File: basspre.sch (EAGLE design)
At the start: 6 parts, among them IC1 LF351D

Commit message: initial layout
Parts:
- removed R1: 1M5, resistor:R-US_R0603
- removed U$1: LM4250, russell_random:LM4250
- added C102, C104, C107: 1uF, resistor:C-USC0603
- added C103: 1800 pF, resistor:C-USC0603
- added C105, C108: 120pf, resistor:C-USC0603
- added C106: 500pF, resistor:C-USC0603
- added C201, C202, C203, C204: .1uF, resistor:C-USC0603
- added R102: 220K, resistor:R-US_R0603
- added R103: 100K, resistor:R-US_R0603
- added R104: 1.5M, resistor:R-US_R0603
- added SV1: (no value), con-lstb:MA09-1
- added TP1, TP2, TP3: TPPAD1-13, testpad:TPPAD1-13
- added U103: LM4250, russell_random:LM4250
- R101: value 1M5 -> 1.5 M
- renumbered C1 to C101, IC1 to U102, R2 to R101, U$2 to U101
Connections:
- new net BASS1: C108.2, R103.2, SV1.5
- new net BASS2: C105.1, C106.2, C107.2, C108.1, SV1.4, TP3.TP, U103.OUT
- new net N$1: C102.1, C103.2, R102.2
- new net OUTPUT: C107.1, SV1.6
- new net TREBLE1: C106.1, SV1.3
- new net TREBLE2: C104.1, C105.2, R102.1, R103.1, SV1.2, U103.-IN
- new net TREBLE3: C103.1, SV1.1
- net GND: now also C104.2, C201.2, C202.2, C203.2, C204.2, R104.2, SV1.8, U103.V-; no longer R1.2, U$1.V-
- net INPUT: now also SV1.7
- net N$2: now also R104.1, U103.CURRENT; no longer R1.1, U$1.CURRENT
- net N$3: now also C102.2, TP2.TP
- net V+: now also C202.1, C203.1, C204.1, SV1.9, U103.V+; no longer U$1.V+
- net VGND: now also C201.1, TP1.TP, U103.+IN; no longer U$1.+IN
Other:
- note added: "Bypass"
- note added: "Connections"
- note added: "EQ"

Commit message: fix up values
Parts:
- C108: value 120pf -> 47nF
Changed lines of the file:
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@@
 <part name="C105" library="resistor" deviceset="C-US" device="C0603" value="120pf"/>
 <part name="R103" library="resistor" deviceset="R-US_" device="R0603" value="100K"/>
-<part name="C108" library="resistor" deviceset="C-US" device="C0603" value="120pf"/>
+<part name="C108" library="resistor" deviceset="C-US" device="C0603" value="47nF"/>
 <part name="C102" library="resistor" deviceset="C-US" device="C0603" value="1uF"/>
 <part name="R102" library="resistor" deviceset="R-US_" device="R0603" value="220K"/>

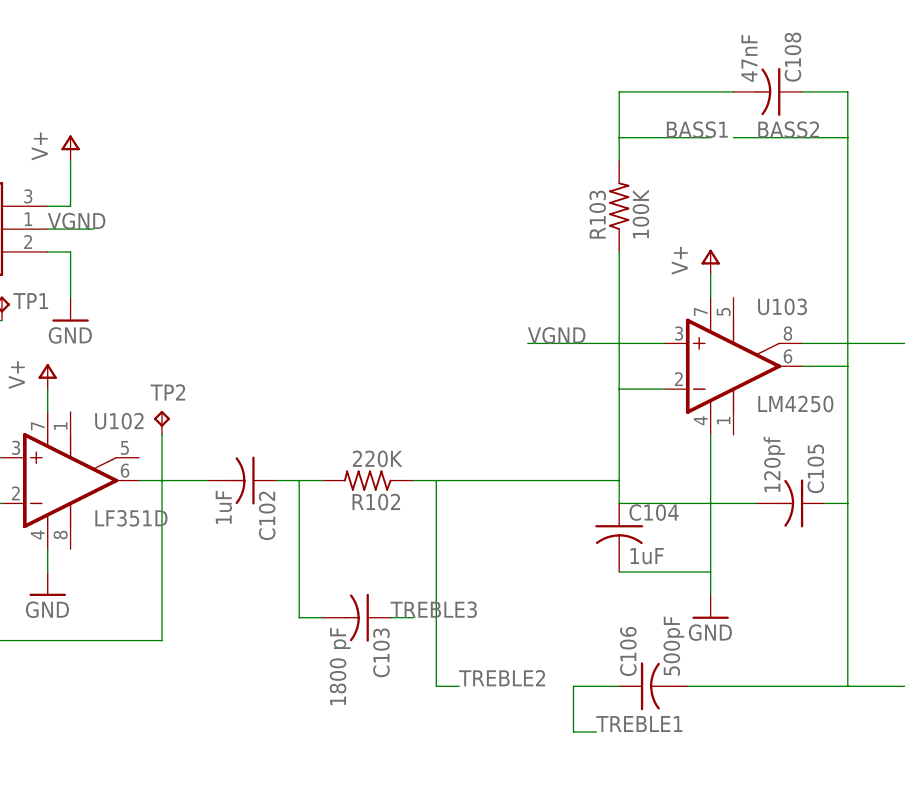
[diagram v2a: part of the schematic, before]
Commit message: added simulations, changed some values around
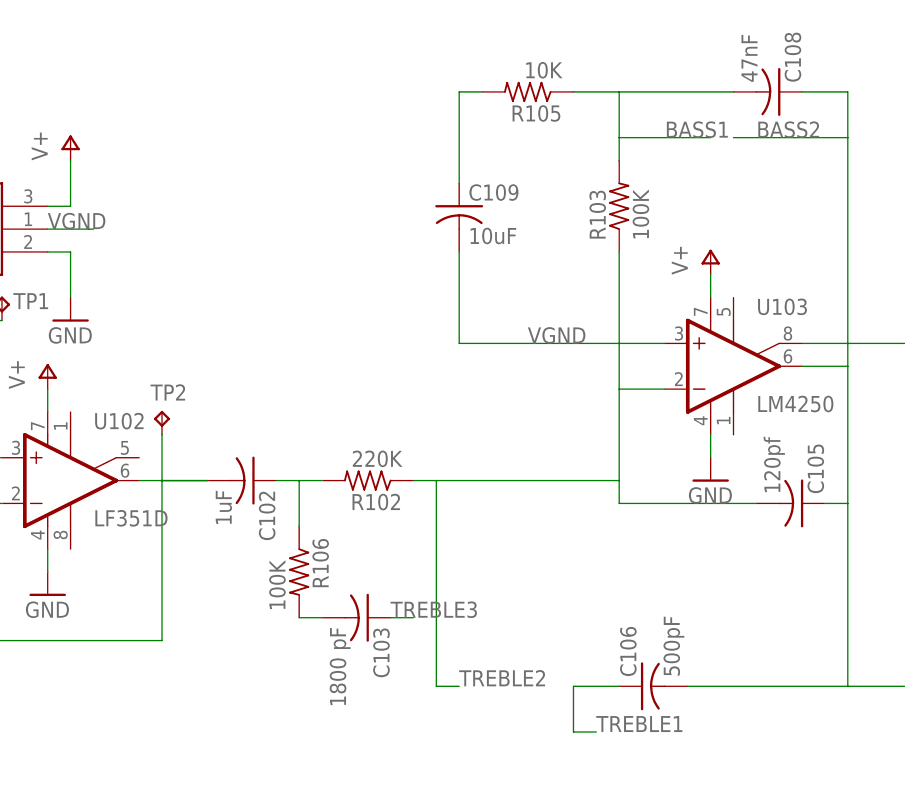
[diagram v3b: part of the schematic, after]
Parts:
- removed C104: 1uF, resistor:C-USC0603
- added C109: 10uF, resistor:C-USC0603
- added R105: 10K, resistor:R-US_R0603
- added R106: 100K, resistor:R-US_R0603
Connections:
- new net N$4: C109.1, R105.2
- new net N$5: C103.2, R106.2
- net BASS1: now also R105.1
- net GND: no longer C104.2
- net N$1: now also R106.1; no longer C103.2
- net TREBLE2: no longer C104.1
- net VGND: now also C109.2
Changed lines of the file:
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@@
 <part name="C101" library="resistor" deviceset="C-US" device="C0603" value="1uF"/>
 <part name="R101" library="resistor" deviceset="R-US_" device="R0603" value="1.5 M"/>
-<part name="C104" library="resistor" deviceset="C-US" device="C0603" value="1uF"/>
 <part name="C105" library="resistor" deviceset="C-US" device="C0603" value="120pf"/>
 <part name="R103" library="resistor" deviceset="R-US_" device="R0603" value="100K"/>
@@
 <part name="P+4" library="supply1" deviceset="V+" device=""/>
 <part name="GND6" library="supply1" deviceset="GND" device=""/>
+<part name="R105" library="resistor" deviceset="R-US_" device="R0603" value="10K"/>
+<part name="C109" library="resistor" deviceset="C-US" device="C0603" value="10uF"/>
+<part name="R106" library="resistor" deviceset="R-US_" device="R0603" value="100K"/>
 </parts>
 <sheets>
@@
 <instance part="U103" gate="G$1" x="114.3" y="149.86"/>
 <instance part="U101" gate="G$1" x="25.4" y="162.56"/>
-<instance part="GND2" gate="1" x="109.22" y="119.38"/>
+<instance part="GND2" gate="1" x="109.22" y="134.62"/>
 <instance part="P+2" gate="1" x="38.1" y="172.72"/>
 <instance part="P+1" gate="1" x="109.22" y="160.02"/>
@@
 <instance part="C101" gate="G$1" x="17.78" y="137.16" rot="R270"/>
 <instance part="R101" gate="G$1" x="25.4" y="144.78" rot="R90"/>
-<instance part="C104" gate="G$1" x="99.06" y="129.54"/>
 <instance part="C105" gate="G$1" x="119.38" y="132.08" rot="MR90"/>
 <instance part="R103" gate="G$1" x="99.06" y="165.1" rot="R90"/>
@@
 <instance part="P+4" gate="1" x="195.58" y="182.88"/>
 <instance part="GND6" gate="1" x="195.58" y="165.1"/>
+<instance part="R105" gate="G$1" x="88.9" y="177.8" rot="R180"/>
+<instance part="C109" gate="G$1" x="81.28" y="165.1"/>
+<instance part="R106" gate="G$1" x="63.5" y="124.46" smashed="yes" rot="R270">
+<attribute name="NAME" x="64.9986" y="128.27" size="1.778" layer="95" rot="R270"/>
+<attribute name="VALUE" x="60.198" y="125.73" size="1.778" layer="96" rot="R270"/>
+</instance>
 </instances>
 <busses>
@@
 <pinref part="GND2" gate="1" pin="GND"/>
 <pinref part="U103" gate="G$1" pin="V-"/>
-<wire x1="109.22" y1="121.92" x2="109.22" y2="124.46" width="0.1524" layer="91"/>
-<pinref part="C104" gate="G$1" pin="2"/>
-<wire x1="109.22" y1="124.46" x2="109.22" y2="139.7" width="0.1524" layer="91"/>
-<wire x1="99.06" y1="124.46" x2="109.22" y2="124.46" width="0.1524" layer="91"/>
+<wire x1="109.22" y1="137.16" x2="109.22" y2="139.7" width="0.1524" layer="91"/>
 </segment>
 <segment>
@@
 <segment>
 <pinref part="U103" gate="G$1" pin="+IN"/>
-<wire x1="104.14" y1="149.86" x2="88.9" y2="149.86" width="0.1524" layer="91"/>
+<wire x1="104.14" y1="149.86" x2="81.28" y2="149.86" width="0.1524" layer="91"/>
 <label x="88.9" y="149.86" size="1.778" layer="95"/>
+<pinref part="C109" gate="G$1" pin="2"/>
+<wire x1="81.28" y1="160.02" x2="81.28" y2="149.86" width="0.1524" layer="91"/>
 </segment>
 <segment>
@@
 <pinref part="TP2" gate="G$1" pin="TP"/>
 <wire x1="48.26" y1="134.62" x2="48.26" y2="139.7" width="0.1524" layer="91"/>
+<wire x1="48.26" y1="134.62" x2="53.34" y2="134.62" width="0.1524" layer="91"/>
 </segment>
 </net>
@@
 <pinref part="U103" gate="G$1" pin="-IN"/>
 <wire x1="104.14" y1="144.78" x2="99.06" y2="144.78" width="0.1524" layer="91"/>
-<pinref part="C104" gate="G$1" pin="1"/>
 <wire x1="99.06" y1="144.78" x2="99.06" y2="134.62" width="0.1524" layer="91"/>
 <pinref part="C105" gate="G$1" pin="2"/>
@@
 <wire x1="99.06" y1="172.72" x2="109.22" y2="172.72" width="0.1524" layer="91"/>
 <label x="104.14" y="172.72" size="1.778" layer="95"/>
+<pinref part="R105" gate="G$1" pin="1"/>
+<wire x1="99.06" y1="177.8" x2="93.98" y2="177.8" width="0.1524" layer="91"/>
 </segment>
 <segment>
@@
 <pinref part="R102" gate="G$1" pin="2"/>
 <wire x1="60.96" y1="134.62" x2="63.5" y2="134.62" width="0.1524" layer="91"/>
+<pinref part="R106" gate="G$1" pin="1"/>
 <wire x1="63.5" y1="134.62" x2="66.04" y2="134.62" width="0.1524" layer="91"/>
-<wire x1="63.5" y1="134.62" x2="63.5" y2="119.38" width="0.1524" layer="91"/>
-<pinref part="C103" gate="G$1" pin="2"/>
-<wire x1="63.5" y1="119.38" x2="66.04" y2="119.38" width="0.1524" layer="91"/>
+<wire x1="63.5" y1="129.54" x2="63.5" y2="134.62" width="0.1524" layer="91"/>
 </segment>
 </net>
@@
 </segment>
 </net>
+<net name="N$4" class="0">
+<segment>
+<pinref part="C109" gate="G$1" pin="1"/>
+<wire x1="81.28" y1="167.64" x2="81.28" y2="177.8" width="0.1524" layer="91"/>
+<pinref part="R105" gate="G$1" pin="2"/>
+<wire x1="81.28" y1="177.8" x2="83.82" y2="177.8" width="0.1524" layer="91"/>
+</segment>
+</net>
+<net name="N$5" class="0">
+<segment>
+<pinref part="C103" gate="G$1" pin="2"/>
+<wire x1="63.5" y1="119.38" x2="66.04" y2="119.38" width="0.1524" layer="91"/>
+<pinref part="R106" gate="G$1" pin="2"/>
+</segment>
+</net>

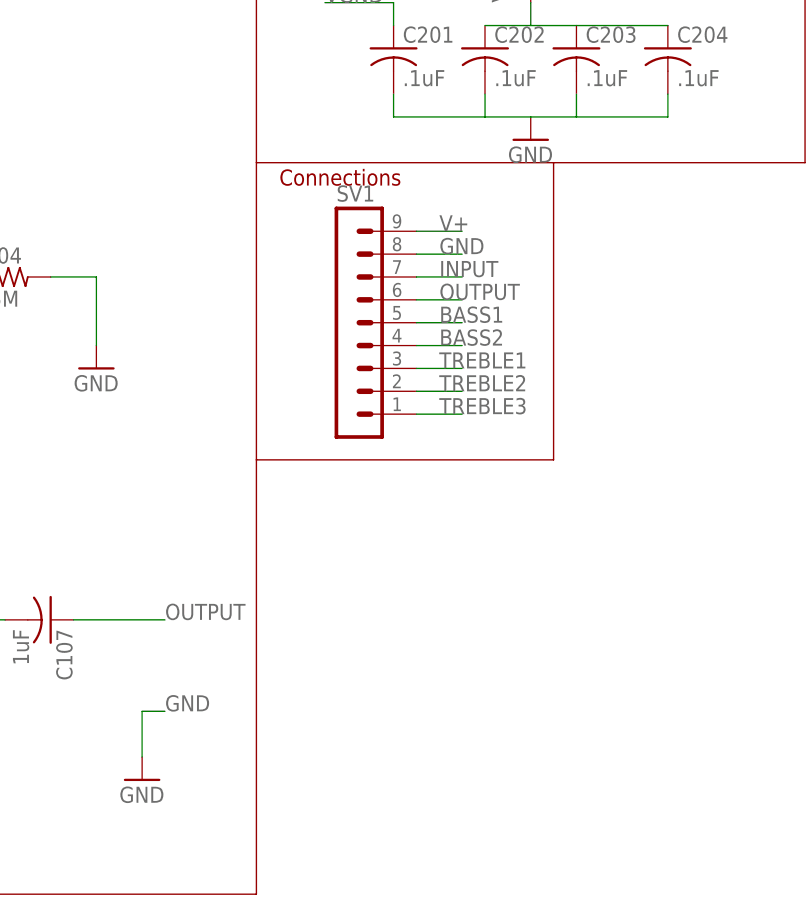
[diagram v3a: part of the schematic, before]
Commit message: switched to 10 pin system so bass pot can be three terminal in future revisions without changing connection.
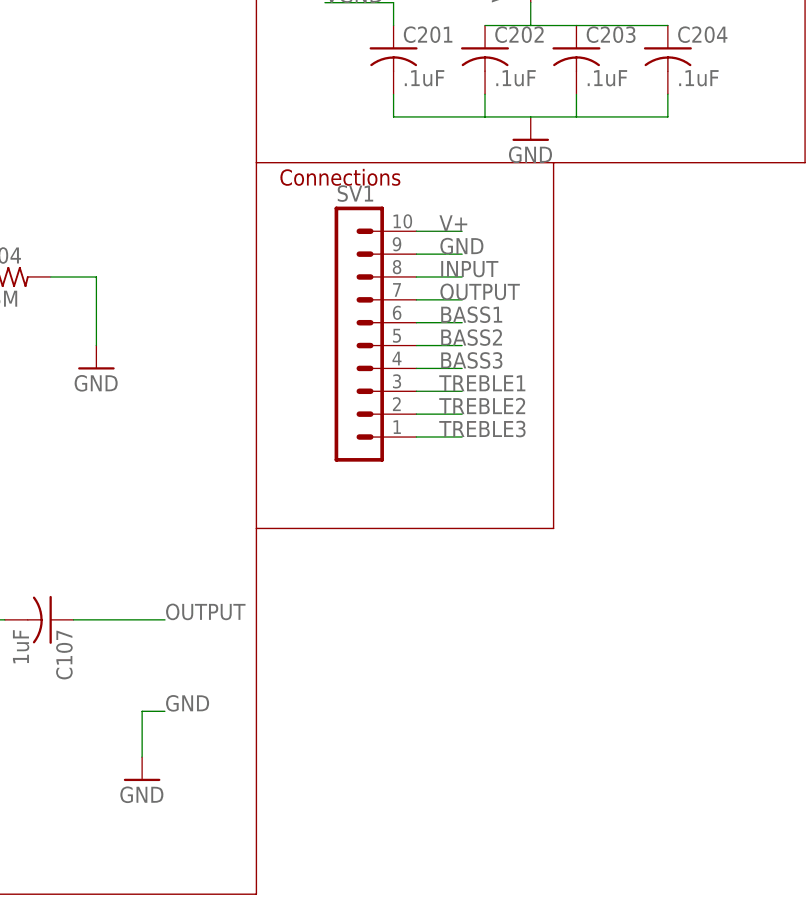
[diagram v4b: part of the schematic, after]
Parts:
- SV1: device con-lstb:MA09-1 -> con-lstb:MA10-1
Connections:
- new net BASS3: SV1.4
- net BASS1: now also SV1.6; no longer SV1.5
- net BASS2: now also SV1.5; no longer SV1.4
- net GND: now also SV1.9; no longer SV1.8
- net INPUT: now also SV1.8; no longer SV1.7
- net OUTPUT: now also SV1.7; no longer SV1.6
- net V+: now also SV1.10; no longer SV1.9
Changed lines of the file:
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@@
 <part name="C203" library="resistor" deviceset="C-US" device="C0603" value=".1uF"/>
 <part name="C204" library="resistor" deviceset="C-US" device="C0603" value=".1uF"/>
-<part name="SV1" library="con-lstb" deviceset="MA09-1" device=""/>
+<part name="SV1" library="con-lstb" deviceset="MA10-1" device=""/>
 <part name="P+4" library="supply1" deviceset="V+" device=""/>
 <part name="GND6" library="supply1" deviceset="GND" device=""/>
@@
 <plain>
 <wire x1="0" y1="81.28" x2="165.1" y2="81.28" width="0.1524" layer="94"/>
-<wire x1="165.1" y1="81.28" x2="165.1" y2="129.54" width="0.1524" layer="94"/>
-<wire x1="165.1" y1="129.54" x2="165.1" y2="162.56" width="0.1524" layer="94"/>
+<wire x1="165.1" y1="81.28" x2="165.1" y2="121.92" width="0.1524" layer="94"/>
+<wire x1="165.1" y1="121.92" x2="165.1" y2="162.56" width="0.1524" layer="94"/>
 <wire x1="165.1" y1="162.56" x2="165.1" y2="185.42" width="0.1524" layer="94"/>
 <wire x1="165.1" y1="162.56" x2="198.12" y2="162.56" width="0.1524" layer="94"/>
@@
 <text x="2.54" y="182.88" size="1.778" layer="94">EQ</text>
 <text x="167.64" y="182.88" size="1.778" layer="94">Bypass</text>
-<wire x1="165.1" y1="129.54" x2="198.12" y2="129.54" width="0.1524" layer="94"/>
-<wire x1="198.12" y1="129.54" x2="198.12" y2="162.56" width="0.1524" layer="94"/>
+<wire x1="165.1" y1="121.92" x2="198.12" y2="121.92" width="0.1524" layer="94"/>
+<wire x1="198.12" y1="121.92" x2="198.12" y2="162.56" width="0.1524" layer="94"/>
 <text x="167.64" y="160.02" size="1.778" layer="94">Connections</text>
 </plain>
@@
 <instance part="C203" gate="G$1" x="200.66" y="175.26"/>
 <instance part="C204" gate="G$1" x="210.82" y="175.26"/>
-<instance part="SV1" gate="1" x="175.26" y="144.78"/>
+<instance part="SV1" gate="1" x="175.26" y="142.24"/>
 <instance part="P+4" gate="1" x="195.58" y="182.88"/>
 <instance part="GND6" gate="1" x="195.58" y="165.1"/>
@@
 </segment>
 <segment>
-<pinref part="SV1" gate="1" pin="8"/>
-<wire x1="182.88" y1="152.4" x2="187.96" y2="152.4" width="0.1524" layer="91"/>
-<label x="185.42" y="152.4" size="1.778" layer="95"/>
-</segment>
-<segment>
 <pinref part="C204" gate="G$1" pin="2"/>
 <wire x1="210.82" y1="170.18" x2="210.82" y2="167.64" width="0.1524" layer="91"/>
@@
 <wire x1="200.66" y1="170.18" x2="200.66" y2="167.64" width="0.1524" layer="91"/>
 </segment>
+<segment>
+<pinref part="SV1" gate="1" pin="9"/>
+<wire x1="182.88" y1="152.4" x2="187.96" y2="152.4" width="0.1524" layer="91"/>
+<label x="185.42" y="152.4" size="1.778" layer="95"/>
+</segment>
 </net>
 <net name="V+" class="0">
@@
 <pinref part="P+3" gate="1" pin="V+"/>
 <wire x1="35.56" y1="144.78" x2="35.56" y2="142.24" width="0.1524" layer="91"/>
-</segment>
-<segment>
-<pinref part="SV1" gate="1" pin="9"/>
-<wire x1="182.88" y1="154.94" x2="187.96" y2="154.94" width="0.1524" layer="91"/>
-<label x="185.42" y="154.94" size="1.778" layer="95"/>
 </segment>
 <segment>
@@
 <pinref part="C204" gate="G$1" pin="1"/>
 <wire x1="200.66" y1="177.8" x2="210.82" y2="177.8" width="0.1524" layer="91"/>
+</segment>
+<segment>
+<pinref part="SV1" gate="1" pin="10"/>
+<wire x1="182.88" y1="154.94" x2="187.96" y2="154.94" width="0.1524" layer="91"/>
+<label x="185.42" y="154.94" size="1.778" layer="95"/>
 </segment>
 </net>
@@
 </segment>
 <segment>
-<pinref part="SV1" gate="1" pin="7"/>
+<pinref part="SV1" gate="1" pin="8"/>
 <wire x1="182.88" y1="149.86" x2="187.96" y2="149.86" width="0.1524" layer="91"/>
 <label x="185.42" y="149.86" size="1.778" layer="95"/>
@@
 </segment>
 <segment>
-<pinref part="SV1" gate="1" pin="4"/>
+<pinref part="SV1" gate="1" pin="5"/>
 <wire x1="182.88" y1="142.24" x2="187.96" y2="142.24" width="0.1524" layer="91"/>
 <label x="185.42" y="142.24" size="1.778" layer="95"/>
@@
 <segment>
 <pinref part="SV1" gate="1" pin="2"/>
-<wire x1="182.88" y1="137.16" x2="187.96" y2="137.16" width="0.1524" layer="91"/>
-<label x="185.42" y="137.16" size="1.778" layer="95"/>
+<wire x1="182.88" y1="134.62" x2="187.96" y2="134.62" width="0.1524" layer="91"/>
+<label x="185.42" y="134.62" size="1.778" layer="95"/>
 </segment>
 </net>
@@
 </segment>
 <segment>
-<pinref part="SV1" gate="1" pin="5"/>
+<pinref part="SV1" gate="1" pin="6"/>
 <wire x1="182.88" y1="144.78" x2="187.96" y2="144.78" width="0.1524" layer="91"/>
 <label x="185.42" y="144.78" size="1.778" layer="95"/>
@@
 <segment>
 <pinref part="SV1" gate="1" pin="1"/>
-<wire x1="182.88" y1="134.62" x2="187.96" y2="134.62" width="0.1524" layer="91"/>
-<label x="185.42" y="134.62" size="1.778" layer="95"/>
+<wire x1="182.88" y1="132.08" x2="187.96" y2="132.08" width="0.1524" layer="91"/>
+<label x="185.42" y="132.08" size="1.778" layer="95"/>
 </segment>
 </net>
@@
 <segment>
 <pinref part="SV1" gate="1" pin="3"/>
-<wire x1="182.88" y1="139.7" x2="187.96" y2="139.7" width="0.1524" layer="91"/>
-<label x="185.42" y="139.7" size="1.778" layer="95"/>
+<wire x1="182.88" y1="137.16" x2="187.96" y2="137.16" width="0.1524" layer="91"/>
+<label x="185.42" y="137.16" size="1.778" layer="95"/>
 </segment>
 </net>
 <net name="OUTPUT" class="0">
-<segment>
-<pinref part="SV1" gate="1" pin="6"/>
-<wire x1="182.88" y1="147.32" x2="187.96" y2="147.32" width="0.1524" layer="91"/>
-<label x="185.42" y="147.32" size="1.778" layer="95"/>
-</segment>
 <segment>
 <pinref part="C107" gate="G$1" pin="1"/>
 <wire x1="144.78" y1="111.76" x2="154.94" y2="111.76" width="0.1524" layer="91"/>
 <label x="154.94" y="111.76" size="1.778" layer="95"/>
+</segment>
+<segment>
+<pinref part="SV1" gate="1" pin="7"/>
+<wire x1="182.88" y1="147.32" x2="187.96" y2="147.32" width="0.1524" layer="91"/>
+<label x="185.42" y="147.32" size="1.778" layer="95"/>
 </segment>
 </net>
@@
 </segment>
 </net>
+<net name="BASS3" class="0">
+<segment>
+<pinref part="SV1" gate="1" pin="4"/>
+<wire x1="182.88" y1="139.7" x2="187.96" y2="139.7" width="0.1524" layer="91"/>
+<label x="185.42" y="139.7" size="1.778" layer="95"/>
+</segment>
+</net>
